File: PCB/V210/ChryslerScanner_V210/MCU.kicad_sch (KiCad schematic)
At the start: 26 parts, among them Q1 UMH3N, SW1 RESET, SW2 BOOT, U1 ESP32-PICO-D4, U2 PI4IOE5V6416ZDEX

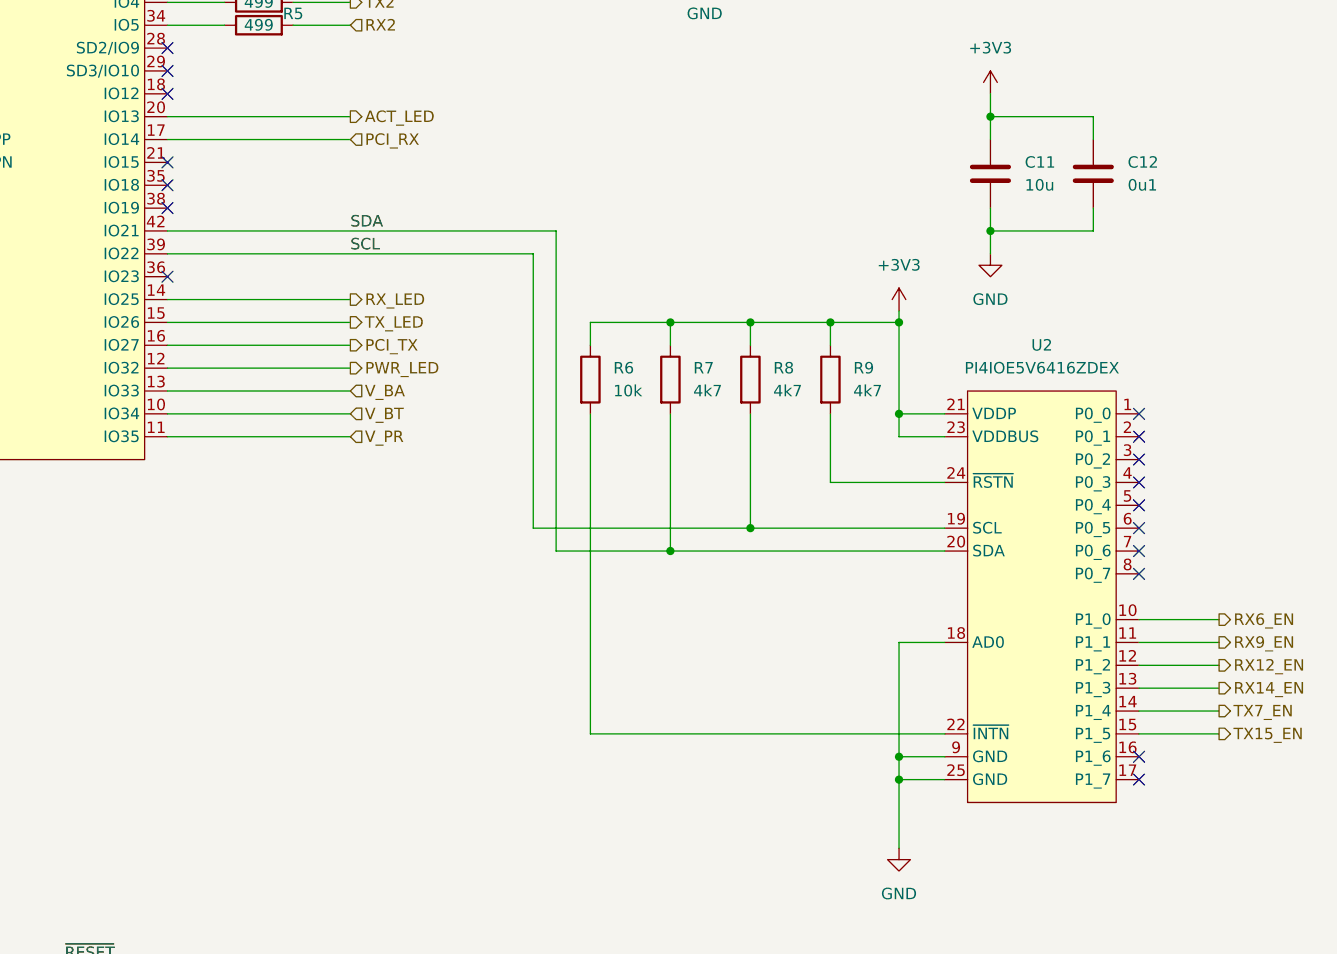
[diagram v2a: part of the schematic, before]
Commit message: Added CCD back in - needed for early TJs.
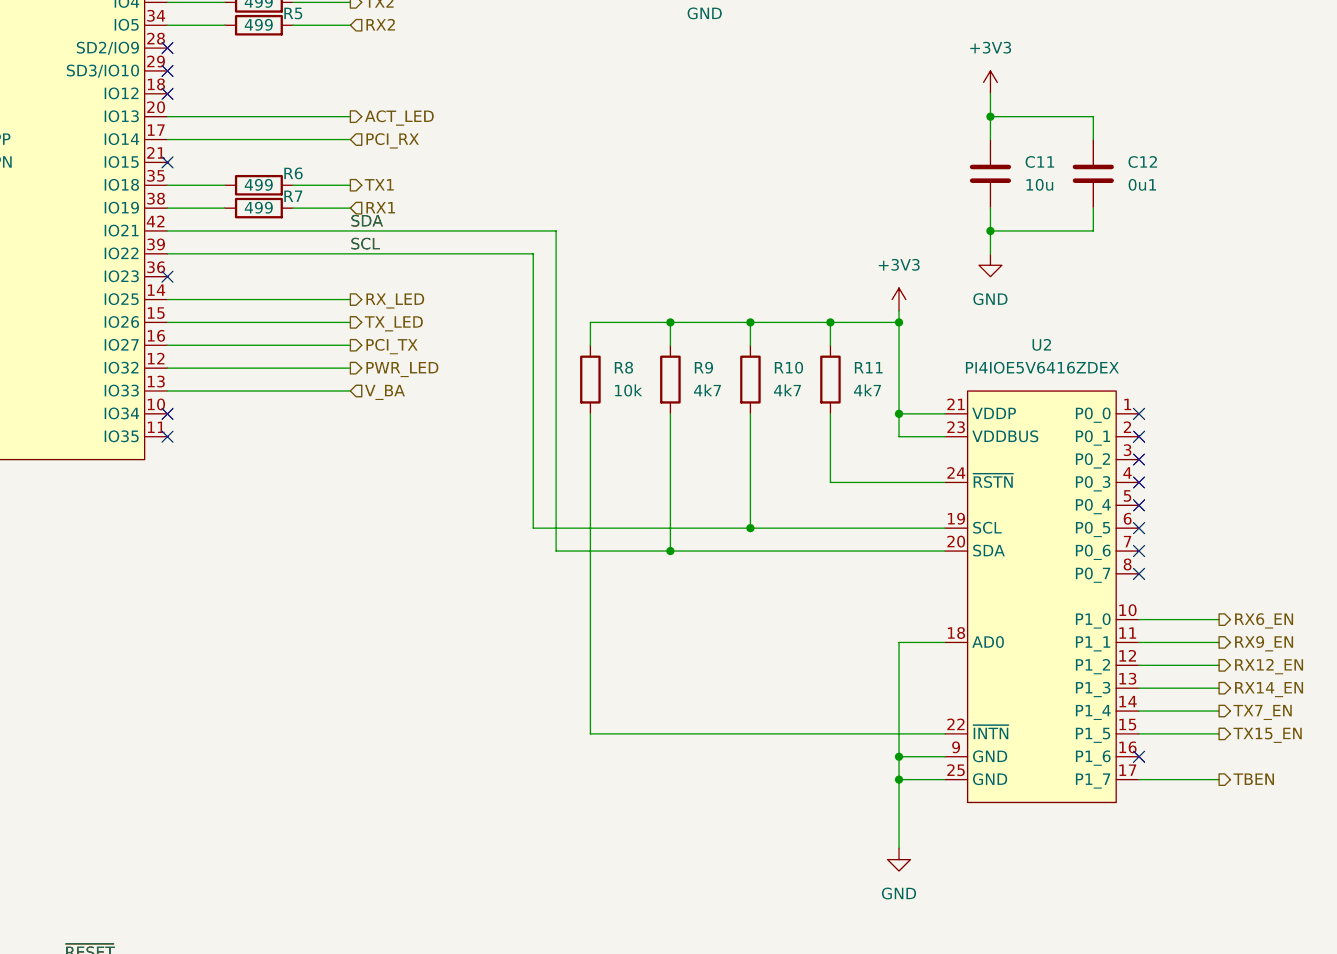
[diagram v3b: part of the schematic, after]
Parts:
- added R6, R7: 499, Resistor_SMD:R_0603_1608Metric, symbol Device:R
- renumbered R8 to R10, R9 to R11, R6 to R8, R7 to R9
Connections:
- net TBEN: now reaches U2.17 (P1_7)
- net at U1.35 (IO18): now also R6.1
- net at U1.38 (IO19): now also R7.1
- net V_BT: no longer names the net of U1.10 (IO34)
- net V_PR: no longer names the net of U1.11 (IO35)
- new net RX1: R7.2
- new net TX1: R6.2
- no-connect marks 29 -> 28
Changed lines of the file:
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@@
   (title_block
     (title "TJ Diag")
-    (date "2023-07-06")
+    (date "2023-07-07")
     (rev "V1.00")
     (company "andy@britishideas.com")
@@
   (junction (at 81.28 68.58) (diameter 0) (color 0 0 0 0)
   )
+  (no_connect (at 149.86 92.71))
+  (no_connect (at 149.86 95.25))
   (no_connect (at 149.86 77.47))
-  (no_connect (at 149.86 67.31))
-  (no_connect (at 149.86 69.85))
   (no_connect (at 257.81 130.81))
-  (no_connect (at 257.81 133.35))
   (no_connect (at 116.84 74.93))
   (no_connect (at 116.84 77.47))
@@
     (stroke (width 0) (type default) (color 0 0 0 0))
   )
+  (wire (pts (xy 149.86 69.85) (xy 156.21 69.85))
+    (stroke (width 0) (type default) (color 0 0 0 0))
+  )
   (wire (pts (xy 196.85 128.27) (xy 236.22 128.27))
     (stroke (width 0) (type default) (color 0 0 0 0))
@@
     (stroke (width 0) (type default) (color 0 0 0 0))
   )
+  (wire (pts (xy 257.81 133.35) (xy 266.7 133.35))
+    (stroke (width 0) (type default) (color 0 0 0 0))
+  )
   (wire (pts (xy 69.85 176.53) (xy 73.66 176.53))
     (stroke (width 0) (type default) (color 0 0 0 0))
@@
     (stroke (width 0) (type default) (color 0 0 0 0))
   )
+  (wire (pts (xy 163.83 69.85) (xy 170.18 69.85))
+    (stroke (width 0) (type default) (color 0 0 0 0))
+  )
   (wire (pts (xy 214.63 105.41) (xy 214.63 92.71))
     (stroke (width 0) (type default) (color 0 0 0 0))
@@
     (stroke (width 0) (type default) (color 0 0 0 0))
   )
+  (wire (pts (xy 163.83 67.31) (xy 170.18 67.31))
+    (stroke (width 0) (type default) (color 0 0 0 0))
+  )
   (wire (pts (xy 231.14 133.35) (xy 236.22 133.35))
     (stroke (width 0) (type default) (color 0 0 0 0))
@@
     (stroke (width 0) (type default) (color 0 0 0 0))
   )
-  (wire (pts (xy 149.86 95.25) (xy 170.18 95.25))
-    (stroke (width 0) (type default) (color 0 0 0 0))
-  )
-  (wire (pts (xy 149.86 92.71) (xy 170.18 92.71))
+  (wire (pts (xy 149.86 67.31) (xy 156.21 67.31))
     (stroke (width 0) (type default) (color 0 0 0 0))
   )
@@
     (effects (font (size 1.27 1.27)) (justify right bottom))
   )
-  (hierarchical_label "V_PR" (shape input) (at 170.18 95.25 0)
-    (effects (font (size 1.27 1.27)) (justify left))
-  )
   (hierarchical_label "TX7_EN" (shape output) (at 266.7 125.73 0)
     (effects (font (size 1.27 1.27)) (justify left))
   )
+  (hierarchical_label "RX1" (shape input) (at 170.18 69.85 0)
+    (effects (font (size 1.27 1.27)) (justify left))
+  )
   (hierarchical_label "RX2" (shape input) (at 170.18 49.53 0)
     (effects (font (size 1.27 1.27)) (justify left))
   )
   (hierarchical_label "TX_LED" (shape output) (at 170.18 82.55 0)
+    (effects (font (size 1.27 1.27)) (justify left))
+  )
+  (hierarchical_label "TX1" (shape output) (at 170.18 67.31 0)
     (effects (font (size 1.27 1.27)) (justify left))
   )
@@
     (effects (font (size 1.27 1.27)) (justify left))
   )
+  (hierarchical_label "TBEN" (shape output) (at 266.7 133.35 0)
+    (effects (font (size 1.27 1.27)) (justify left))
+  )
   (hierarchical_label "RX12_EN" (shape output) (at 266.7 120.65 0)
     (effects (font (size 1.27 1.27)) (justify left))
@@
     (effects (font (size 1.27 1.27)) (justify left))
   )
-  (hierarchical_label "V_BT" (shape input) (at 170.18 92.71 0)
-    (effects (font (size 1.27 1.27)) (justify left))
-  )
   (symbol (lib_id "power:+3V3") (at 241.3 57.15 0) (unit 1)
     (in_bom yes) (on_board yes) (fields_autoplaced)
@@
     )
     (pin "1")
+  )
+  (symbol (lib_id "Device:R") (at 160.02 69.85 90) (unit 1)
+    (in_bom yes) (on_board yes)
+    (property "Reference" "R7" (id 0) (at 163.83 68.58 90))
+    (property "Value" "499" (id 1) (at 160.02 69.85 90))
+    (property "Footprint" "Resistor_SMD:R_0603_1608Metric" (id 2) (at 160.02 71.628 90)
+      (effects (font (size 1.27 1.27)) hide)
+    )
+    (property "Datasheet" "~" (id 3) (at 160.02 69.85 0)
+      (effects (font (size 1.27 1.27)) hide)
+    )
+    (pin "1")
+    (pin "2")
   )
   (symbol (lib_id "power:GND") (at 69.85 86.36 0) (unit 1)
@@
   (symbol (lib_id "Device:R") (at 214.63 88.9 0) (unit 1)
     (in_bom yes) (on_board yes) (fields_autoplaced)
-    (property "Reference" "R8" (id 0) (at 217.17 87.6299 0)
+    (property "Reference" "R10" (id 0) (at 217.17 87.6299 0)
       (effects (font (size 1.27 1.27)) (justify left))
     )
@@
   (symbol (lib_id "Device:R") (at 196.85 88.9 0) (unit 1)
     (in_bom yes) (on_board yes) (fields_autoplaced)
-    (property "Reference" "R6" (id 0) (at 199.39 87.6299 0)
+    (property "Reference" "R8" (id 0) (at 199.39 87.6299 0)
       (effects (font (size 1.27 1.27)) (justify left))
     )
@@
   (symbol (lib_id "Device:R") (at 205.74 88.9 0) (unit 1)
     (in_bom yes) (on_board yes) (fields_autoplaced)
-    (property "Reference" "R7" (id 0) (at 208.28 87.6299 0)
+    (property "Reference" "R9" (id 0) (at 208.28 87.6299 0)
       (effects (font (size 1.27 1.27)) (justify left))
     )
@@
     (pin "2")
   )
+  (symbol (lib_id "Device:R") (at 160.02 67.31 90) (unit 1)
+    (in_bom yes) (on_board yes)
+    (property "Reference" "R6" (id 0) (at 163.83 66.04 90))
+    (property "Value" "499" (id 1) (at 160.02 67.31 90))
+    (property "Footprint" "Resistor_SMD:R_0603_1608Metric" (id 2) (at 160.02 69.088 90)
+      (effects (font (size 1.27 1.27)) hide)
+    )
+    (property "Datasheet" "~" (id 3) (at 160.02 67.31 0)
+      (effects (font (size 1.27 1.27)) hide)
+    )
+    (pin "1")
+    (pin "2")
+  )
   (symbol (lib_id "Device:R") (at 160.02 46.99 90) (unit 1)
     (in_bom yes) (on_board yes)
@@
   (symbol (lib_id "Device:R") (at 223.52 88.9 0) (unit 1)
     (in_bom yes) (on_board yes) (fields_autoplaced)
-    (property "Reference" "R9" (id 0) (at 226.06 87.6299 0)
-      (effects (font (size 1.27 1.27)) (justify left))
-    )
+    (property "Reference" "R11" (id 0) (at 226.06 87.6299 0)
+      (effects (font (size 1.27 1.27)) (justify left))
+    )

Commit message: Working on PCB layout.
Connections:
- net +3V3: now also U1.4 (VDDA3P3), U1.43 (VDDA), U1.46 (VDDA)
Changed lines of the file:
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@@
   (title_block
     (title "TJ Diag")
-    (date "2023-07-18")
+    (date "2023-09-12")
     (rev "V1.00")
     (company "andy@britishideas.com")
@@
   (junction (at 57.15 36.83) (diameter 0) (color 0 0 0 0)
   )
+  (junction (at 114.3 46.99) (diameter 0) (color 0 0 0 0)
+  )
   (junction (at 101.6 104.14) (diameter 0) (color 0 0 0 0)
   )
@@
   (junction (at 114.3 39.37) (diameter 0) (color 0 0 0 0)
   )
+  (junction (at 114.3 44.45) (diameter 0) (color 0 0 0 0)
+  )
   (junction (at 114.3 41.91) (diameter 0) (color 0 0 0 0)
   )
@@
   (junction (at 241.3 59.69) (diameter 0) (color 0 0 0 0)
   )
+  (junction (at 114.3 49.53) (diameter 0) (color 0 0 0 0)
+  )
   (junction (at 114.3 36.83) (diameter 0) (color 0 0 0 0)
   )
@@
   (junction (at 81.28 68.58) (diameter 0) (color 0 0 0 0)
   )
+  (no_connect (at 116.84 68.58))
+  (no_connect (at 116.84 66.04))
+  (no_connect (at 116.84 63.5))
+  (no_connect (at 116.84 60.96))
+  (no_connect (at 116.84 58.42))
   (no_connect (at 149.86 92.71))
   (no_connect (at 149.86 95.25))
@@
   (no_connect (at 116.84 77.47))
   (no_connect (at 116.84 82.55))
-  (no_connect (at 116.84 67.31))
   (no_connect (at 116.84 72.39))
   (no_connect (at 116.84 80.01))
-  (no_connect (at 116.84 59.69))
-  (no_connect (at 116.84 64.77))
   (no_connect (at 116.84 85.09))
-  (no_connect (at 116.84 62.23))
   (no_connect (at 149.86 41.91))
   (no_connect (at 149.86 52.07))
@@
   (no_connect (at 257.81 100.33))
   (no_connect (at 257.81 97.79))
-  (no_connect (at 116.84 54.61))
   (wire (pts (xy 252.73 59.69) (xy 241.3 59.69))
     (stroke (width 0) (type default) (color 0 0 0 0))
@@
     (stroke (width 0) (type default) (color 0 0 0 0))
   )
+  (wire (pts (xy 114.3 46.99) (xy 116.84 46.99))
+    (stroke (width 0) (type default) (color 0 0 0 0))
+  )
   (wire (pts (xy 257.81 133.35) (xy 266.7 133.35))
     (stroke (width 0) (type default) (color 0 0 0 0))
@@
     (stroke (width 0) (type default) (color 0 0 0 0))
   )
+  (wire (pts (xy 116.84 52.07) (xy 114.3 52.07))
+    (stroke (width 0) (type default) (color 0 0 0 0))
+  )
   (wire (pts (xy 196.85 82.55) (xy 196.85 85.09))
     (stroke (width 0) (type default) (color 0 0 0 0))
@@
     (stroke (width 0) (type default) (color 0 0 0 0))
   )
+  (wire (pts (xy 111.76 55.88) (xy 116.84 55.88))
+    (stroke (width 0) (type default) (color 0 0 0 0))
+  )
   (wire (pts (xy 69.85 138.43) (xy 73.66 138.43))
     (stroke (width 0) (type default) (color 0 0 0 0))
@@
     (stroke (width 0) (type default) (color 0 0 0 0))
   )
+  (wire (pts (xy 114.3 46.99) (xy 114.3 44.45))
+    (stroke (width 0) (type default) (color 0 0 0 0))
+  )
   (wire (pts (xy 163.83 44.45) (xy 170.18 44.45))
     (stroke (width 0) (type default) (color 0 0 0 0))
@@
     (stroke (width 0) (type default) (color 0 0 0 0))
   )
-  (wire (pts (xy 113.03 52.07) (xy 116.84 52.07))
-    (stroke (width 0) (type default) (color 0 0 0 0))
-  )
   (wire (pts (xy 77.47 36.83) (xy 67.31 36.83))
     (stroke (width 0) (type default) (color 0 0 0 0))
   )
+  (wire (pts (xy 114.3 52.07) (xy 114.3 49.53))
+    (stroke (width 0) (type default) (color 0 0 0 0))
+  )
   (wire (pts (xy 223.52 82.55) (xy 231.14 82.55))
     (stroke (width 0) (type default) (color 0 0 0 0))
@@
     (stroke (width 0) (type default) (color 0 0 0 0))
   )
+  (wire (pts (xy 114.3 49.53) (xy 114.3 46.99))
+    (stroke (width 0) (type default) (color 0 0 0 0))
+  )
   (wire (pts (xy 163.83 46.99) (xy 170.18 46.99))
     (stroke (width 0) (type default) (color 0 0 0 0))
@@
   )
   (wire (pts (xy 163.83 49.53) (xy 170.18 49.53))
+    (stroke (width 0) (type default) (color 0 0 0 0))
+  )
+  (wire (pts (xy 114.3 49.53) (xy 116.84 49.53))
     (stroke (width 0) (type default) (color 0 0 0 0))
   )
@@
     (effects (font (size 1.27 1.27)) (justify left bottom))
   )
-  (label "~{RESET}" (at 113.03 52.07 180)
+  (label "~{RESET}" (at 111.76 55.88 180)
     (effects (font (size 1.27 1.27)) (justify right bottom))
   )
@@
   )
   (symbol (lib_id "ChryslerScanner:ESP32-PICO-D4") (at 119.38 67.31 0) (unit 1)
-    (in_bom yes) (on_board yes) (fields_autoplaced)
+    (in_bom yes) (on_board yes)
     (property "Reference" "U1" (id 0) (at 133.35 29.21 0))
     (property "Value" "ESP32-PICO-D4" (id 1) (at 133.35 31.75 0))
@@
     (pin "38")
     (pin "39")
+    (pin "4")
     (pin "40")
     (pin "41")
     (pin "42")
+    (pin "43")
+    (pin "44")
+    (pin "45")
+    (pin "46")
+    (pin "47")
+    (pin "48")
     (pin "49")
     (pin "5")
